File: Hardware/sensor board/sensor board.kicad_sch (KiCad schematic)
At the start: 4 parts, among them J1 Conn_01x04_Pin, J1 Raspberry_Pi_2_3

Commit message: changed symbol references
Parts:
- J2: renamed from Bar1; value ~ -> Bar30; symbol New_Library:Bar30 -> Sensor_Board_Components:Bar30
- J3: renamed from LPS331AP1; value ~ -> LPS331AP; symbol New_Library:LPS331AP -> Sensor_Board_Components:LPS331AP
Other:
- note removed: "CS pulled up to VDD by default = I2C"
- moved on the sheet: J3
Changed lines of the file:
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@@
     (stroke (width 0) (type default))
   )
-  (wire (pts (xy 128.27 134.62) (xy 101.6 134.62))
+  (wire (pts (xy 128.27 135.89) (xy 101.6 135.89))
     (stroke (width 0) (type default))
   )
@@
     (stroke (width 0) (type default))
   )
-  (wire (pts (xy 121.92 142.24) (xy 128.27 142.24))
+  (wire (pts (xy 121.92 143.51) (xy 128.27 143.51))
     (stroke (width 0) (type default))
   )
@@
     (stroke (width 0) (type default))
   )
-  (wire (pts (xy 128.27 138.43) (xy 95.25 138.43))
+  (wire (pts (xy 128.27 139.7) (xy 95.25 139.7))
     (stroke (width 0) (type default))
   )
@@
     (stroke (width 0) (type default))
   )
-  (wire (pts (xy 101.6 91.44) (xy 101.6 134.62))
-    (stroke (width 0) (type default))
-  )
-  (wire (pts (xy 95.25 88.9) (xy 95.25 138.43))
+  (wire (pts (xy 101.6 91.44) (xy 101.6 135.89))
+    (stroke (width 0) (type default))
+  )
+  (wire (pts (xy 95.25 88.9) (xy 95.25 139.7))
     (stroke (width 0) (type default))
   )
@@
     (stroke (width 0) (type default))
   )
-  (wire (pts (xy 121.92 146.05) (xy 128.27 146.05))
-    (stroke (width 0) (type default))
-  )
-  (text "CS pulled up to VDD by default = I2C" (at 173.99 146.05 0)
-    (effects (font (size 1.27 1.27)) (justify left bottom))
+  (wire (pts (xy 121.92 147.32) (xy 128.27 147.32))
+    (stroke (width 0) (type default))
   )
   (label "SDA" (at 85.09 88.9 0) (fields_autoplaced)
@@
   (symbol (lib_id "power:+3.3V") (at 163.83 85.09 270) (unit 1)
     (in_bom yes) (on_board yes) (dnp no) (fields_autoplaced)
-    (property "Reference" "#PWR02" (at 160.02 85.09 0)
+    (property "Reference" "#PWR05" (at 160.02 85.09 0)
       (effects (font (size 1.27 1.27)) hide)
     )
@@
       (project "sensor board"
         (path "/b809390c-5c7b-4faa-a505-ee668295313b"
-          (reference "#PWR02") (unit 1)
+          (reference "#PWR05") (unit 1)
         )
       )
@@
   (symbol (lib_id "power:+3.3V") (at 217.17 116.84 90) (unit 1)
     (in_bom yes) (on_board yes) (dnp no) (fields_autoplaced)
-    (property "Reference" "#PWR05" (at 220.98 116.84 0)
+    (property "Reference" "#PWR08" (at 220.98 116.84 0)
       (effects (font (size 1.27 1.27)) hide)
     )
@@
       (project "sensor board"
         (path "/b809390c-5c7b-4faa-a505-ee668295313b"
-          (reference "#PWR05") (unit 1)
+          (reference "#PWR08") (unit 1)
         )
         (path "/b809390c-5c7b-4faa-a505-ee668295313b/b45961e0-d21c-4cf1-a8fa-4e6b738a8420"
@@
   (symbol (lib_id "power:GND") (at 52.07 140.97 0) (unit 1)
     (in_bom yes) (on_board yes) (dnp no) (fields_autoplaced)
-    (property "Reference" "#PWR06" (at 52.07 147.32 0)
+    (property "Reference" "#PWR01" (at 52.07 147.32 0)
       (effects (font (size 1.27 1.27)) hide)
     )
@@
       (project "sensor board"
         (path "/b809390c-5c7b-4faa-a505-ee668295313b"
-          (reference "#PWR06") (unit 1)
+          (reference "#PWR01") (unit 1)
         )
       )
@@
     )
   )
-  (symbol (lib_id "New_Library:LPS331AP") (at 148.59 130.81 0) (unit 1)
-    (in_bom yes) (on_board yes) (dnp no) (fields_autoplaced)
-    (property "Reference" "LPS331AP1" (at 149.225 130.81 0)
-      (effects (font (size 1.27 1.27)))
-    )
-    (property "Value" "~" (at 148.59 130.81 0)
+  (symbol (lib_id "Sensor_Board_Components:LPS331AP") (at 148.59 130.81 0) (unit 1)
+    (in_bom yes) (on_board yes) (dnp no)
+    (property "Reference" "J3" (at 149.225 130.81 0)
+      (effects (font (size 1.27 1.27)))
+    )
+    (property "Value" "LPS331AP" (at 148.59 156.21 0)
       (effects (font (size 1.27 1.27)))
     )
@@
       (project "sensor board"
         (path "/b809390c-5c7b-4faa-a505-ee668295313b"
+          (reference "J3") (unit 1)
+        )
+      )
+      (project "Sensor Board 3"
+        (path "/f823486c-a1c6-456c-a47c-520c825b8d4c"
           (reference "LPS331AP1") (unit 1)
         )
       )
-      (project "Sensor Board 3"
-        (path "/f823486c-a1c6-456c-a47c-520c825b8d4c"
-          (reference "LPS331AP1") (unit 1)
-        )
-      )
-    )
-  )
-  (symbol (lib_id "power:+3.3V") (at 121.92 146.05 90) (unit 1)
-    (in_bom yes) (on_board yes) (dnp no) (fields_autoplaced)
-    (property "Reference" "#PWR08" (at 125.73 146.05 0)
-      (effects (font (size 1.27 1.27)) hide)
-    )
-    (property "Value" "+3.3V" (at 118.11 146.05 90)
+    )
+  )
+  (symbol (lib_id "power:+3.3V") (at 121.92 147.32 90) (unit 1)
+    (in_bom yes) (on_board yes) (dnp no) (fields_autoplaced)
+    (property "Reference" "#PWR04" (at 125.73 147.32 0)
+      (effects (font (size 1.27 1.27)) hide)
+    )
+    (property "Value" "+3.3V" (at 118.11 147.32 90)
       (effects (font (size 1.27 1.27)) (justify left))
     )
-    (property "Footprint" "" (at 121.92 146.05 0)
-      (effects (font (size 1.27 1.27)) hide)
-    )
-    (property "Datasheet" "" (at 121.92 146.05 0)
-      (effects (font (size 1.27 1.27)) hide)
-    )
-    (pin "1")
-    (instances
-      (project "sensor board"
-        (path "/b809390c-5c7b-4faa-a505-ee668295313b"
-          (reference "#PWR08") (unit 1)
+    (property "Footprint" "" (at 121.92 147.32 0)
+      (effects (font (size 1.27 1.27)) hide)
+    )
+    (property "Datasheet" "" (at 121.92 147.32 0)
+      (effects (font (size 1.27 1.27)) hide)
+    )
+    (pin "1")
+    (instances
+      (project "sensor board"
+        (path "/b809390c-5c7b-4faa-a505-ee668295313b"
+          (reference "#PWR04") (unit 1)
         )
       )
@@
   (symbol (lib_id "power:GND") (at 163.83 91.44 90) (unit 1)
     (in_bom yes) (on_board yes) (dnp no) (fields_autoplaced)
-    (property "Reference" "#PWR03" (at 170.18 91.44 0)
+    (property "Reference" "#PWR06" (at 170.18 91.44 0)
       (effects (font (size 1.27 1.27)) hide)
     )
@@
       (project "sensor board"
         (path "/b809390c-5c7b-4faa-a505-ee668295313b"
-          (reference "#PWR03") (unit 1)
+          (reference "#PWR06") (unit 1)
         )
       )
@@
         )
         (path "/b809390c-5c7b-4faa-a505-ee668295313b"
-          (reference "J2") (unit 1)
-        )
-      )
-    )
-  )
-  (symbol (lib_id "New_Library:Bar30") (at 135.89 96.52 180) (unit 1)
-    (in_bom yes) (on_board yes) (dnp no) (fields_autoplaced)
-    (property "Reference" "Bar1" (at 135.89 96.52 0)
-      (effects (font (size 1.27 1.27)))
-    )
-    (property "Value" "~" (at 135.89 96.52 0)
+          (reference "J4") (unit 1)
+        )
+      )
+    )
+  )
+  (symbol (lib_id "Sensor_Board_Components:Bar30") (at 135.89 96.52 180) (unit 1)
+    (in_bom yes) (on_board yes) (dnp no)
+    (property "Reference" "J2" (at 135.89 80.01 0)
+      (effects (font (size 1.27 1.27)))
+    )
+    (property "Value" "Bar30" (at 137.16 96.52 0)
       (effects (font (size 1.27 1.27)))
     )
@@
       (effects (font (size 1.27 1.27)) hide)
     )
-    (pin "4")
     (pin "1")
     (pin "2")
     (pin "3")
-    (instances
-      (project "sensor board"
-        (path "/b809390c-5c7b-4faa-a505-ee668295313b"
-          (reference "Bar1") (unit 1)
+    (pin "4")
+    (instances
+      (project "sensor board"
+        (path "/b809390c-5c7b-4faa-a505-ee668295313b"
+          (reference "J2") (unit 1)
         )
       )
@@
   (symbol (lib_id "power:+3.3V") (at 64.77 67.31 0) (unit 1)
     (in_bom yes) (on_board yes) (dnp no) (fields_autoplaced)
-    (property "Reference" "#PWR01" (at 64.77 71.12 0)
+    (property "Reference" "#PWR02" (at 64.77 71.12 0)
       (effects (font (size 1.27 1.27)) hide)
     )
@@
       (project "sensor board"
         (path "/b809390c-5c7b-4faa-a505-ee668295313b"
-          (reference "#PWR01") (unit 1)
+          (reference "#PWR02") (unit 1)
         )
       )
@@
     )
   )
-  (symbol (lib_id "power:GND") (at 121.92 142.24 270) (unit 1)
-    (in_bom yes) (on_board yes) (dnp no) (fields_autoplaced)
-    (property "Reference" "#PWR07" (at 115.57 142.24 0)
-      (effects (font (size 1.27 1.27)) hide)
-    )
-    (property "Value" "GND" (at 118.11 142.24 90)
+  (symbol (lib_id "power:GND") (at 121.92 143.51 270) (unit 1)
+    (in_bom yes) (on_board yes) (dnp no) (fields_autoplaced)
+    (property "Reference" "#PWR03" (at 115.57 143.51 0)
+      (effects (font (size 1.27 1.27)) hide)
+    )
+    (property "Value" "GND" (at 118.11 143.51 90)
       (effects (font (size 1.27 1.27)) (justify right))
     )
-    (property "Footprint" "" (at 121.92 142.24 0)
-      (effects (font (size 1.27 1.27)) hide)
-    )
-    (property "Datasheet" "" (at 121.92 142.24 0)
-      (effects (font (size 1.27 1.27)) hide)
-    )
-    (pin "1")
-    (instances
-      (project "sensor board"
-        (path "/b809390c-5c7b-4faa-a505-ee668295313b"
-          (reference "#PWR07") (unit 1)
+    (property "Footprint" "" (at 121.92 143.51 0)
+      (effects (font (size 1.27 1.27)) hide)
+    )
+    (property "Datasheet" "" (at 121.92 143.51 0)
+      (effects (font (size 1.27 1.27)) hide)
+    )
+    (pin "1")
+    (instances
+      (project "sensor board"
+        (path "/b809390c-5c7b-4faa-a505-ee668295313b"
+          (reference "#PWR03") (unit 1)
         )
       )
@@
         )
         (path "/b809390c-5c7b-4faa-a505-ee668295313b"
-          (reference "#PWR04") (unit 1)
-        )
-      )
+          (reference "#PWR07") (unit 1)
+        )
+      )

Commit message: Added footprints to connectors
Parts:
- J1: footprint (none) -> Connector_JST:JST_XH_B4B-XH-AM_1x04_P2.50mm_Vertical
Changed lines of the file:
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@@
       (effects (font (size 1.27 1.27)))
     )
-    (property "Footprint" "" (at 227.33 114.3 0)
+    (property "Footprint" "Connector_JST:JST_XH_B4B-XH-AM_1x04_P2.50mm_Vertical" (at 227.33 114.3 0)
       (effects (font (size 1.27 1.27)) hide)
     )

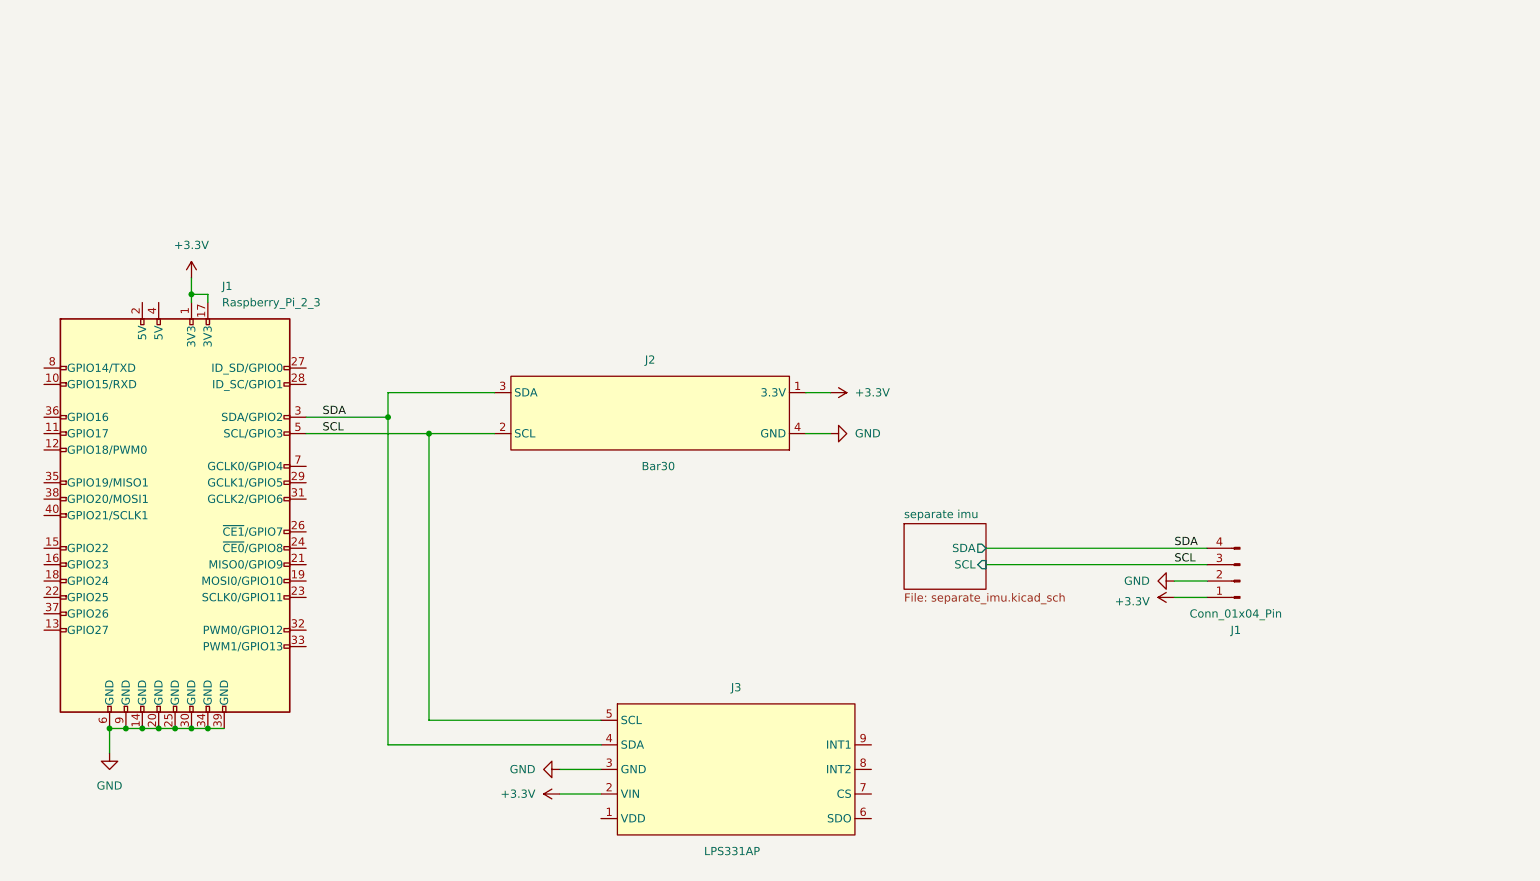
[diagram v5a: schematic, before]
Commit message: updated sensor board pcb with footprints
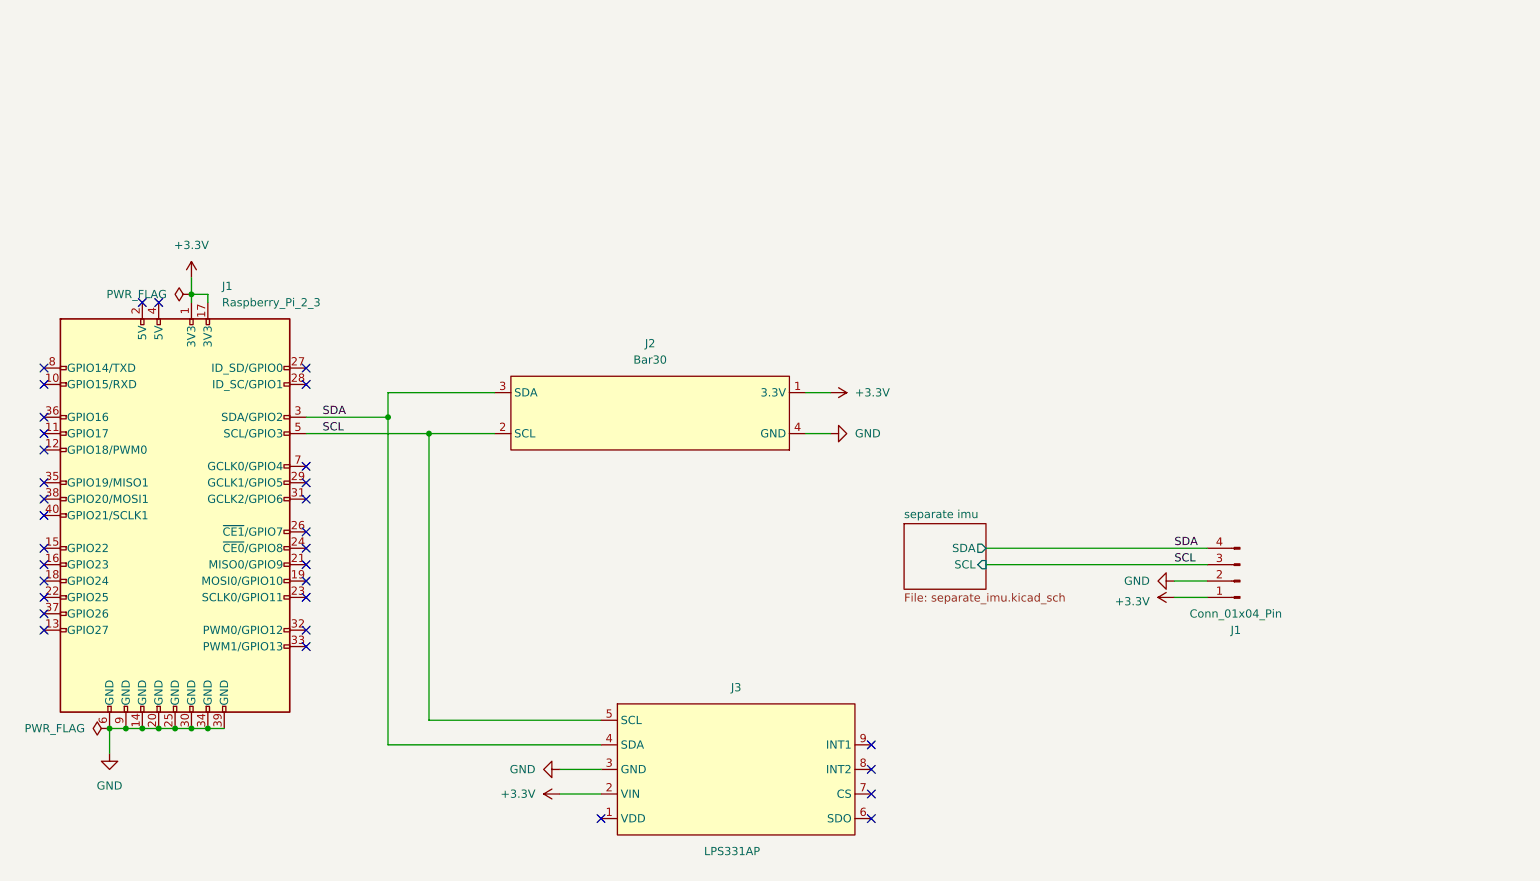
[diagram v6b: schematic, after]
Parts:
- J1: footprint (none) -> Connector_PinHeader_2.54mm:PinHeader_2x20_P2.54mm_Vertical
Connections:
- no-connect marks 0 -> 33
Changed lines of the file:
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@@
   (junction (at 64.77 137.16) (diameter 0) (color 0 0 0 0)
   )
+  (no_connect (at 170.18 151.13))
+  (no_connect (at 41.91 104.14))
+  (no_connect (at 57.15 71.12))
+  (no_connect (at 82.55 81.28))
+  (no_connect (at 41.91 93.98))
+  (no_connect (at 82.55 124.46))
+  (no_connect (at 41.91 114.3))
+  (no_connect (at 82.55 111.76))
+  (no_connect (at 41.91 101.6))
+  (no_connect (at 82.55 114.3))
+  (no_connect (at 82.55 109.22))
+  (no_connect (at 41.91 91.44))
+  (no_connect (at 59.69 71.12))
+  (no_connect (at 41.91 88.9))
+  (no_connect (at 170.18 139.7))
+  (no_connect (at 41.91 116.84))
+  (no_connect (at 82.55 99.06))
+  (no_connect (at 41.91 121.92))
+  (no_connect (at 128.27 151.13))
+  (no_connect (at 170.18 143.51))
+  (no_connect (at 41.91 81.28))
+  (no_connect (at 41.91 119.38))
+  (no_connect (at 41.91 109.22))
+  (no_connect (at 82.55 96.52))
+  (no_connect (at 41.91 99.06))
+  (no_connect (at 170.18 147.32))
+  (no_connect (at 82.55 101.6))
+  (no_connect (at 41.91 111.76))
+  (no_connect (at 82.55 116.84))
+  (no_connect (at 82.55 121.92))
+  (no_connect (at 82.55 106.68))
+  (no_connect (at 82.55 83.82))
+  (no_connect (at 41.91 83.82))
   (wire (pts (xy 67.31 69.85) (xy 64.77 69.85))
     (stroke (width 0) (type default))
@@
   (label "SCL" (at 217.17 111.76 0) (fields_autoplaced)
     (effects (font (size 1.27 1.27)) (justify left bottom))
+  )
+  (symbol (lib_name "Bar30_1") (lib_id "Sensor_Board_Components:Bar30") (at 135.89 96.52 180) (unit 1)
+    (in_bom yes) (on_board yes) (dnp no) (fields_autoplaced)
+    (property "Reference" "J2" (at 135.89 77.47 0)
+      (effects (font (size 1.27 1.27)))
+    )
+    (property "Value" "Bar30" (at 135.89 80.01 0)
+      (effects (font (size 1.27 1.27)))
+    )
+    (property "Footprint" "Connector_JST:JST_GH_BM04B-GHS-TBT_1x04-1MP_P1.25mm_Vertical" (at 135.89 96.52 0)
+      (effects (font (size 1.27 1.27)) hide)
+    )
+    (property "Datasheet" "" (at 135.89 96.52 0)
+      (effects (font (size 1.27 1.27)) hide)
+    )
+    (pin "1")
+    (pin "2")
+    (pin "3")
+    (pin "4")
+    (instances
+      (project "sensor board"
+        (path "/b809390c-5c7b-4faa-a505-ee668295313b"
+          (reference "J2") (unit 1)
+        )
+      )
+    )
   )
   (symbol (lib_id "power:+3.3V") (at 163.83 85.09 270) (unit 1)
@@
     )
   )
+  (symbol (lib_id "PCM_4ms_Power-symbol:PWR_FLAG") (at 64.77 69.85 90) (unit 1)
+    (in_bom yes) (on_board yes) (dnp no) (fields_autoplaced)
+    (property "Reference" "#FLG01" (at 62.865 69.85 0)
+      (effects (font (size 1.27 1.27)) hide)
+    )
+    (property "Value" "PWR_FLAG" (at 60.96 69.85 90)
+      (effects (font (size 1.27 1.27)) (justify left))
+    )
+    (property "Footprint" "" (at 64.77 69.85 0)
+      (effects (font (size 1.27 1.27)) hide)
+    )
+    (property "Datasheet" "" (at 64.77 69.85 0)
+      (effects (font (size 1.27 1.27)) hide)
+    )
+    (pin "1")
+    (instances
+      (project "sensor board"
+        (path "/b809390c-5c7b-4faa-a505-ee668295313b"
+          (reference "#FLG01") (unit 1)
+        )
+      )
+    )
+  )
   (symbol (lib_id "power:+3.3V") (at 121.92 147.32 90) (unit 1)
     (in_bom yes) (on_board yes) (dnp no) (fields_autoplaced)
@@
     )
   )
-  (symbol (lib_id "Sensor_Board_Components:Bar30") (at 135.89 96.52 180) (unit 1)
-    (in_bom yes) (on_board yes) (dnp no)
-    (property "Reference" "J2" (at 135.89 80.01 0)
-      (effects (font (size 1.27 1.27)))
-    )
-    (property "Value" "Bar30" (at 137.16 96.52 0)
-      (effects (font (size 1.27 1.27)))
-    )
-    (property "Footprint" "Connector_JST:JST_GH_BM04B-GHS-TBT_1x04-1MP_P1.25mm_Vertical" (at 135.89 96.52 0)
-      (effects (font (size 1.27 1.27)) hide)
-    )
-    (property "Datasheet" "" (at 135.89 96.52 0)
-      (effects (font (size 1.27 1.27)) hide)
-    )
-    (pin "1")
-    (pin "2")
-    (pin "3")
-    (pin "4")
-    (instances
-      (project "sensor board"
-        (path "/b809390c-5c7b-4faa-a505-ee668295313b"
-          (reference "J2") (unit 1)
-        )
-      )
-      (project "Sensor Board 3"
-        (path "/f823486c-a1c6-456c-a47c-520c825b8d4c"
-          (reference "Bar1") (unit 1)
+  (symbol (lib_id "PCM_4ms_Power-symbol:PWR_FLAG") (at 52.07 137.16 90) (unit 1)
+    (in_bom yes) (on_board yes) (dnp no) (fields_autoplaced)
+    (property "Reference" "#FLG02" (at 50.165 137.16 0)
+      (effects (font (size 1.27 1.27)) hide)
+    )
+    (property "Value" "PWR_FLAG" (at 48.26 137.16 90)
+      (effects (font (size 1.27 1.27)) (justify left))
+    )
+    (property "Footprint" "" (at 52.07 137.16 0)
+      (effects (font (size 1.27 1.27)) hide)
+    )
+    (property "Datasheet" "" (at 52.07 137.16 0)
+      (effects (font (size 1.27 1.27)) hide)
+    )
+    (pin "1")
+    (instances
+      (project "sensor board"
+        (path "/b809390c-5c7b-4faa-a505-ee668295313b"
+          (reference "#FLG02") (unit 1)
         )
       )
@@
       (effects (font (size 1.27 1.27)) (justify left))
     )
-    (property "Footprint" "" (at 62.23 104.14 0)
-      (effects (font (size 1.27 1.27)) hide)
-    )
+    (property "Footprint" "Connector_PinHeader_2.54mm:PinHeader_2x20_P2.54mm_Vertical" (at 62.23 104.14 0)
+      (effects (font (size 1.27 1.27)) hide)
+    )

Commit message: updated 3d models
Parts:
- J1: footprint Connector_JST:JST_XH_B4B-XH-AM_1x04_P2.50mm_Vertical -> Connector_JST:JST_XH_B4B-XH-A_1x04_P2.50mm_Vertical
- J1: footprint Connector_PinHeader_2.54mm:PinHeader_2x20_P2.54mm_Vertical -> Connector_PinSocket_2.54mm:PinSocket_2x20_P2.54mm_Vertical
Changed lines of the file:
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@@
       (effects (font (size 1.27 1.27)))
     )
-    (property "Footprint" "Connector_JST:JST_XH_B4B-XH-AM_1x04_P2.50mm_Vertical" (at 227.33 114.3 0)
+    (property "Footprint" "Connector_JST:JST_XH_B4B-XH-A_1x04_P2.50mm_Vertical" (at 227.33 114.3 0)
       (effects (font (size 1.27 1.27)) hide)
     )
@@
       (effects (font (size 1.27 1.27)) (justify left))
     )
-    (property "Footprint" "Connector_PinHeader_2.54mm:PinHeader_2x20_P2.54mm_Vertical" (at 62.23 104.14 0)
+    (property "Footprint" "Connector_PinSocket_2.54mm:PinSocket_2x20_P2.54mm_Vertical" (at 62.23 104.14 0)
       (effects (font (size 1.27 1.27)) hide)
     )
